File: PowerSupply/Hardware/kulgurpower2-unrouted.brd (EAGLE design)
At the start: 102 x 86.5 mm, 182 parts, among them M1 MST2V, M2 MST2V, M3 MST2V, M4 MST2V, Q1 BSH103, Q2 BSH103, Q3 BSH103, Q4 BSH103, X1 1727036, X2 2534-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

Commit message: Schematic component type fixes
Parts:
- LED1, LED2, LED3, LED4, LED5, LED6: value GREEN -> BLUE
- PWRLED: value YELLOW -> BLUE
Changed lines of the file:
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@@
 <attribute name="NAME" x="62.985" y="75.604" size="1.778" layer="25" ratio="10"/>
 </element>
-<element name="LED1" library="led" package="CHIP-LED0603" value="GREEN" x="28.0392" y="76.9295" smashed="yes" rot="R180"/>
-<element name="LED2" library="led" package="CHIP-LED0603" value="GREEN" x="39.7553" y="76.8937" smashed="yes" rot="R180"/>
-<element name="LED3" library="led" package="CHIP-LED0603" value="GREEN" x="51.4579" y="77.0816" smashed="yes" rot="R180"/>
-<element name="LED4" library="led" package="CHIP-LED0603" value="GREEN" x="63.1858" y="77.0688" smashed="yes" rot="R180"/>
-<element name="PWRLED" library="led" package="CHIP-LED0603" value="YELLOW" x="78.5921" y="3.35" smashed="yes" rot="R180"/>
+<element name="LED1" library="led" package="CHIP-LED0603" value="BLUE" x="28.0392" y="76.9295" smashed="yes" rot="R180"/>
+<element name="LED2" library="led" package="CHIP-LED0603" value="BLUE" x="39.7553" y="76.8937" smashed="yes" rot="R180"/>
+<element name="LED3" library="led" package="CHIP-LED0603" value="BLUE" x="51.4579" y="77.0816" smashed="yes" rot="R180"/>
+<element name="LED4" library="led" package="CHIP-LED0603" value="BLUE" x="63.1858" y="77.0688" smashed="yes" rot="R180"/>
+<element name="PWRLED" library="led" package="CHIP-LED0603" value="BLUE" x="78.5921" y="3.35" smashed="yes" rot="R180"/>
 <element name="R12" library="rcl" package="R0603" value="3k" x="78.5937" y="7.0145" smashed="yes" rot="R90"/>
 <element name="R6" library="rcl" package="R0603" value="3k" x="28.0386" y="74.0664" smashed="yes" rot="R90"/>
@@
 <element name="F1" library="SparkFun-PowerIC" package="PTC-1206" value="10A FUSE 1206" x="78.25" y="67.75" smashed="yes" rot="MR90"/>
 <element name="F2" library="SparkFun-PowerIC" package="PTC-1206" value="10A FUSE 1206" x="92.25" y="67.75" smashed="yes" rot="MR90"/>
-<element name="LED5" library="led" package="CHIP-LED0603" value="GREEN" x="81.684" y="76.9923" smashed="yes" rot="R180"/>
+<element name="LED5" library="led" package="CHIP-LED0603" value="BLUE" x="81.684" y="76.9923" smashed="yes" rot="R180"/>
 <element name="R1" library="rcl" package="R0603" value="3k" x="81.752" y="74.0336" smashed="yes" rot="R90"/>
-<element name="LED6" library="led" package="CHIP-LED0603" value="GREEN" x="93.4809" y="77.0252" smashed="yes" rot="R180"/>
+<element name="LED6" library="led" package="CHIP-LED0603" value="BLUE" x="93.4809" y="77.0252" smashed="yes" rot="R180"/>
 <element name="R2" library="rcl" package="R0603" value="3k" x="93.4746" y="74.0719" smashed="yes" rot="R90"/>
 <element name="F3" library="SparkFun-PowerIC" package="PTC-1206" value="10A FUSE 1206" x="20" y="8" smashed="yes" rot="MR270"/>
@@
 </signal>
 </signals>
-<errors>
-</errors>
 </board>
 </drawing>

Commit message: Some values changed in schematic
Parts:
- Q1, Q2, Q3, Q4: value BSH103 -> IRLML6344TRPbF
- R3: value 300k -> 270k
- R31, R32: value 3k16 -> 3k12
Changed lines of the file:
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@@
 <element name="C28" library="rcl" package="C0603" value="0.1" x="50.25" y="16.75" smashed="yes" rot="MR270"/>
 <element name="U$17" library="tps51222" package="QFN-32" value="TPS51222RTVT" x="83.7215" y="34.5885" rot="R90"/>
-<element name="R3" library="rcl" package="R0603" value="300k" x="86.5446" y="25.6307" smashed="yes" rot="R90"/>
+<element name="R3" library="rcl" package="R0603" value="270k" x="86.5446" y="25.6307" smashed="yes" rot="R90"/>
 <element name="R39" library="rcl" package="R0603" value="30k" x="82.1765" y="39.3427" smashed="yes" rot="R180"/>
 <element name="R23" library="rcl" package="R0603" value="18k" x="85.2725" y="39.3453" smashed="yes" rot="R180"/>
@@
 <element name="C17" library="rcl" package="C1210" value="10uF/6.3V" x="72.7084" y="35.9885" smashed="yes" rot="R270"/>
 <element name="SJ104" library="rcl" package="R0603" value="0R" x="77.2764" y="32.9714" smashed="yes" rot="MR0"/>
-<element name="R31" library="rcl" package="R0603" value="3k16" x="88.6898" y="29.6644" smashed="yes" rot="R270"/>
-<element name="R32" library="rcl" package="R0603" value="3k16" x="78.8404" y="29.643" smashed="yes" rot="R270"/>
+<element name="R31" library="rcl" package="R0603" value="3k12" x="88.6898" y="29.6644" smashed="yes" rot="R270"/>
+<element name="R32" library="rcl" package="R0603" value="3k12" x="78.8404" y="29.643" smashed="yes" rot="R270"/>
 <element name="R25" library="rcl" package="R0603" value="100k" x="90.2637" y="32.2263" smashed="yes"/>
 <element name="C16" library="rcl" package="C0603" value="0,1u" x="90.27" y="34.299" smashed="yes" rot="R180"/>
@@
 <element name="R24" library="rcl" package="R0603" value="10k" x="76.95" y="42.35" rot="MR180"/>
 <element name="R26" library="rcl" package="R0603" value="10k" x="65.1" y="41.95" rot="MR180"/>
-<element name="Q1" library="adafruit" package="SOT23" value="BSH103" x="21.5" y="12" smashed="yes" rot="R270">
+<element name="Q1" library="adafruit" package="SOT23" value="IRLML6344TRPbF" x="21.5" y="12" smashed="yes" rot="R270">
 <attribute name="NAME" x="23.405" y="13.905" size="1.27" layer="25" rot="R270"/>
 <attribute name="VALUE" x="18.325" y="13.905" size="1.27" layer="27" rot="R270"/>
@@
 <element name="R29" library="rcl" package="R0603" value="100k" x="18.5" y="12" smashed="yes" rot="R90"/>
 <element name="R30" library="rcl" package="R0603" value="430k" x="18.5" y="15.5" smashed="yes" rot="R90"/>
-<element name="Q2" library="adafruit" package="SOT23" value="BSH103" x="33.5" y="12" rot="R270"/>
+<element name="Q2" library="adafruit" package="SOT23" value="IRLML6344TRPbF" x="33.5" y="12" rot="R270"/>
 <element name="R34" library="rcl" package="R0603" value="430k" x="29" y="15.5" smashed="yes" rot="R90"/>
 <element name="R35" library="rcl" package="R0603" value="100k" x="36" y="14.5" smashed="yes" rot="R180"/>
 <element name="R36" library="rcl" package="R0603" value="100k" x="30.5" y="12" smashed="yes" rot="R90"/>
 <element name="R37" library="rcl" package="R0603" value="430k" x="30.5" y="15.5" smashed="yes" rot="R90"/>
-<element name="Q3" library="adafruit" package="SOT23" value="BSH103" x="45" y="12" rot="R270"/>
+<element name="Q3" library="adafruit" package="SOT23" value="IRLML6344TRPbF" x="45" y="12" rot="R270"/>
 <element name="R38" library="rcl" package="R0603" value="430k" x="40.5" y="15.5" smashed="yes" rot="R90"/>
 <element name="R41" library="rcl" package="R0603" value="100k" x="47.5" y="14.5" smashed="yes" rot="R180"/>
 <element name="R42" library="rcl" package="R0603" value="100k" x="42" y="12" smashed="yes" rot="R90"/>
 <element name="R43" library="rcl" package="R0603" value="430k" x="42" y="15.5" smashed="yes" rot="R90"/>
-<element name="Q4" library="adafruit" package="SOT23" value="BSH103" x="56.5" y="12" rot="R270"/>
+<element name="Q4" library="adafruit" package="SOT23" value="IRLML6344TRPbF" x="56.5" y="12" rot="R270"/>
 <element name="R44" library="rcl" package="R0603" value="430k" x="52" y="15.5" smashed="yes" rot="R90"/>
 <element name="R45" library="rcl" package="R0603" value="100k" x="59" y="14.5" smashed="yes" rot="R180"/>

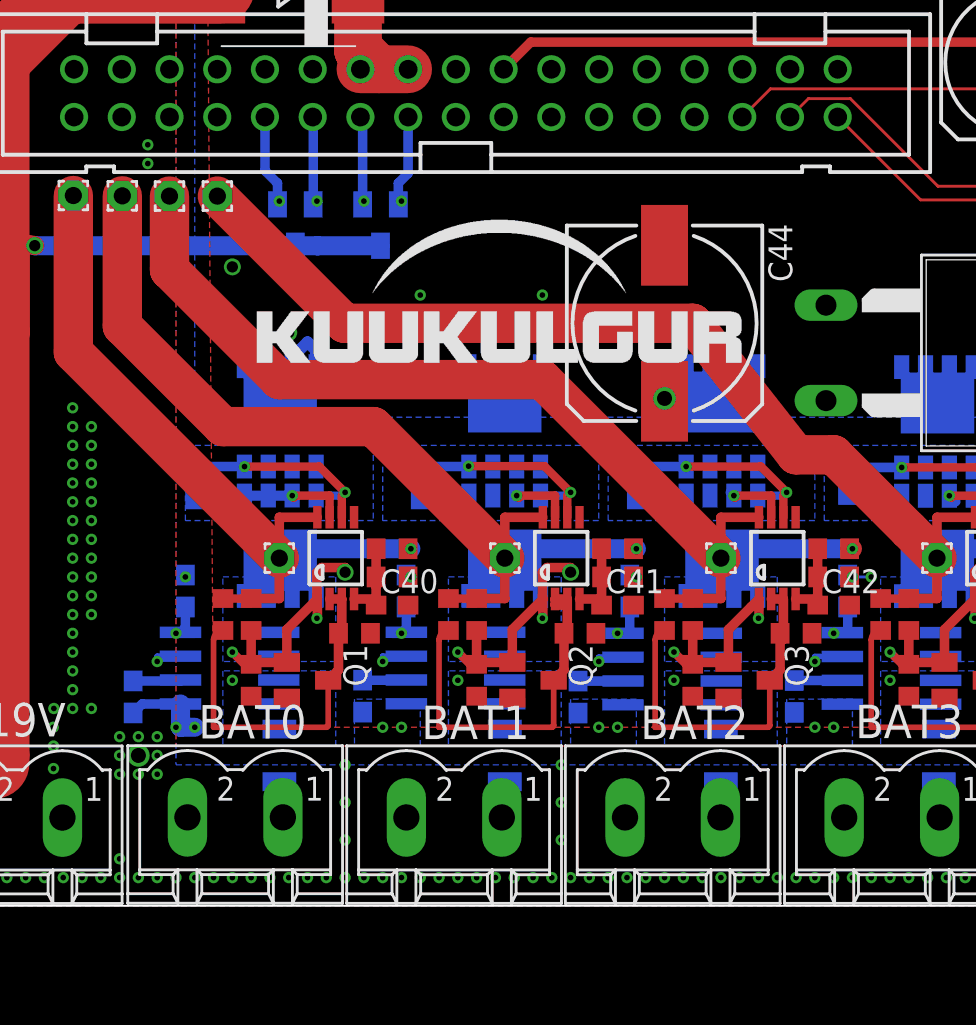
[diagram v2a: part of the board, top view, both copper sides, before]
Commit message: PCB/sch small changes. 19.2Mhz fix additional transistor PSU resistor fixes
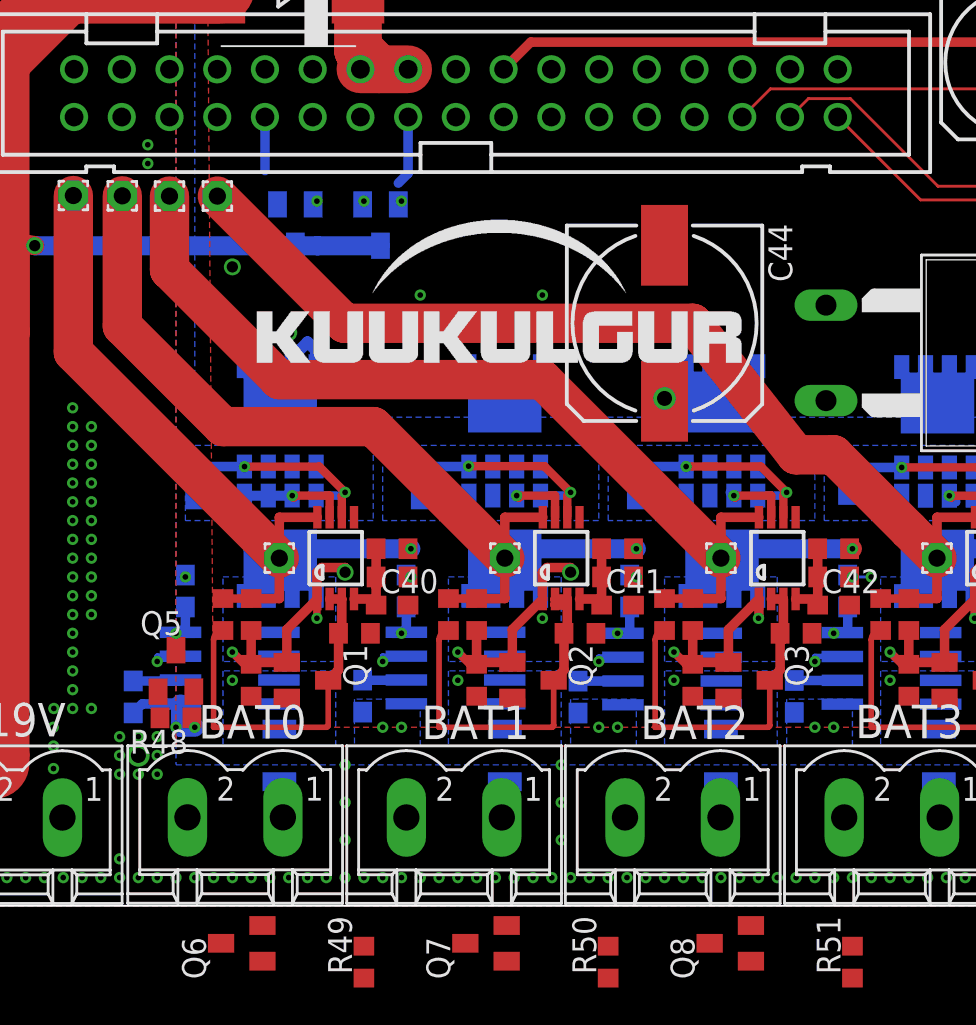
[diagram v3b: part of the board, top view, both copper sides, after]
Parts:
- added Q5, Q6, Q7, Q8: IRLML6344TRPbF, adafruit:SOT23
- added R48, R49, R50, R51: 100k, rcl:R0603
- C13, C14, C44, C45: value 820uF/16V -> 820uF/25V
- C36, C37, C38: value 15V -> 47uF/25V
- C39: value 15v -> 47uF/25V
- F3, F4, F5, F6: value 10A FUSE 1206 -> 15A FUSE 1206
- R25: value 100k -> 3k12
- R29, R36, R42, R46: value 100k -> DNM
- R31: value 3k12 -> 10k
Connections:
- new net !BAT0_EN: D1.1, Q1.1, Q5.3, R29.2, R30.1, U$20.1
- new net !BAT1_EN: D1.2, Q2.1, Q6.3, R36.2, R37.1, U$22.1
- new net !BAT2_EN: D3.1, Q3.1, Q7.3, R42.2, R43.1, U$21.1
- new net !BAT3_EN: D3.2, Q4.1, Q8.3, R46.2, R47.1, U$23.1
- net BAT0_EN: now also Q5.1, R48.2; no longer D1.1, Q1.1, R29.2, R30.1, U$20.1
- net BAT1_EN: now also Q6.1, R49.2; no longer D1.2, Q2.1, R36.2, R37.1, U$22.1
- net BAT2_EN: now also Q7.1, R50.2; no longer D3.1, Q3.1, R42.2, R43.1, U$21.1
- net BAT3_EN: now also Q8.1, R51.2; no longer D3.2, Q4.1, R46.2, R47.1, U$23.1
- net GND: now also Q5.2, Q6.2, Q7.2, Q8.2, R48.1, R49.1, R50.1, R51.1
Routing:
- net BAT3_EN: track 66.0 -> 3.74 mm, vias 4 -> 0
- net !BAT3_EN: track 0.00 -> 61.1 mm, vias 0 -> 4
- net BAT2_EN: track 56.2 -> 0.16 mm, vias 3 -> 0
- net BAT1_EN: track 54.2 -> 0.04 mm, vias 5 -> 0
- net !BAT2_EN: track 0.00 -> 51.3 mm, vias 0 -> 3
- net !BAT1_EN: track 0.00 -> 48.3 mm, vias 0 -> 5
- net BAT0_EN: track 49.0 -> 2.85 mm, vias 5 -> 0
- net !BAT0_EN: track 0.00 -> 43.9 mm, vias 0 -> 4

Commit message: Values changed
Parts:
- R21: value 120k -> 180k
- R32: value 3k12 -> 10k
- R33: value 100k -> 3k12
- R40: value 270k -> 180k
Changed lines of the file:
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@@
 <element name="R4" library="rcl" package="R0603" value="30k" x="90.268" y="38.4427" smashed="yes" rot="R180"/>
 <element name="R5" library="rcl" package="R0603" value="30k" x="77.2929" y="38.4604" smashed="yes"/>
-<element name="R21" library="rcl" package="R0603" value="120k" x="90.2688" y="36.3686" smashed="yes"/>
-<element name="R40" library="rcl" package="R0603" value="270k" x="77.2749" y="36.3829" smashed="yes" rot="R180"/>
+<element name="R21" library="rcl" package="R0603" value="180k" x="90.2688" y="36.3686" smashed="yes"/>
+<element name="R40" library="rcl" package="R0603" value="180k" x="77.2749" y="36.3829" smashed="yes" rot="R180"/>
 <element name="C5" library="rcl" package="C1210" value="10u" x="83.6737" y="24.4193" smashed="yes" rot="R90"/>
 <element name="C21" library="rcl" package="C0603" value="0,1u" x="81.396" y="28.2134" smashed="yes" rot="R180"/>
@@
 <element name="SJ104" library="rcl" package="R0603" value="0R" x="77.2764" y="32.9714" smashed="yes" rot="MR0"/>
 <element name="R31" library="rcl" package="R0603" value="10k" x="88.6898" y="29.6644" smashed="yes" rot="R270"/>
-<element name="R32" library="rcl" package="R0603" value="3k12" x="78.8404" y="29.643" smashed="yes" rot="R270"/>
+<element name="R32" library="rcl" package="R0603" value="10k" x="78.8404" y="29.643" smashed="yes" rot="R270"/>
 <element name="R25" library="rcl" package="R0603" value="3k12" x="90.2637" y="32.2263" smashed="yes"/>
 <element name="C16" library="rcl" package="C0603" value="0,1u" x="90.27" y="34.299" smashed="yes" rot="R180"/>
-<element name="R33" library="rcl" package="R0603" value="100k" x="77.2689" y="32.2297" smashed="yes"/>
+<element name="R33" library="rcl" package="R0603" value="3k12" x="77.2689" y="32.2297" smashed="yes"/>
 <element name="C20" library="rcl" package="C0603" value="0,1u" x="77.2747" y="34.3119" smashed="yes"/>
 <element name="SJ114" library="rcl" package="R0603" value="0R" x="90.7584" y="29.6682" smashed="yes" rot="R270"/>

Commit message: 5V is important
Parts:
- R21: value 180k -> 120k
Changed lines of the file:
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@@
 <element name="R4" library="rcl" package="R0603" value="30k" x="90.268" y="38.4427" smashed="yes" rot="R180"/>
 <element name="R5" library="rcl" package="R0603" value="30k" x="77.2929" y="38.4604" smashed="yes"/>
-<element name="R21" library="rcl" package="R0603" value="180k" x="90.2688" y="36.3686" smashed="yes"/>
+<element name="R21" library="rcl" package="R0603" value="120k" x="90.2688" y="36.3686" smashed="yes"/>
 <element name="R40" library="rcl" package="R0603" value="180k" x="77.2749" y="36.3829" smashed="yes" rot="R180"/>
 <element name="C5" library="rcl" package="C1210" value="10u" x="83.6737" y="24.4193" smashed="yes" rot="R90"/>
